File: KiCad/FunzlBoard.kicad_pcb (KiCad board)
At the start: 2 copper layers, 174 x 149 mm, 56 parts, among them U1 ESP32-C3_SUPERMINI_SMD, U2 ADS7828, U3 MCP23017_SO

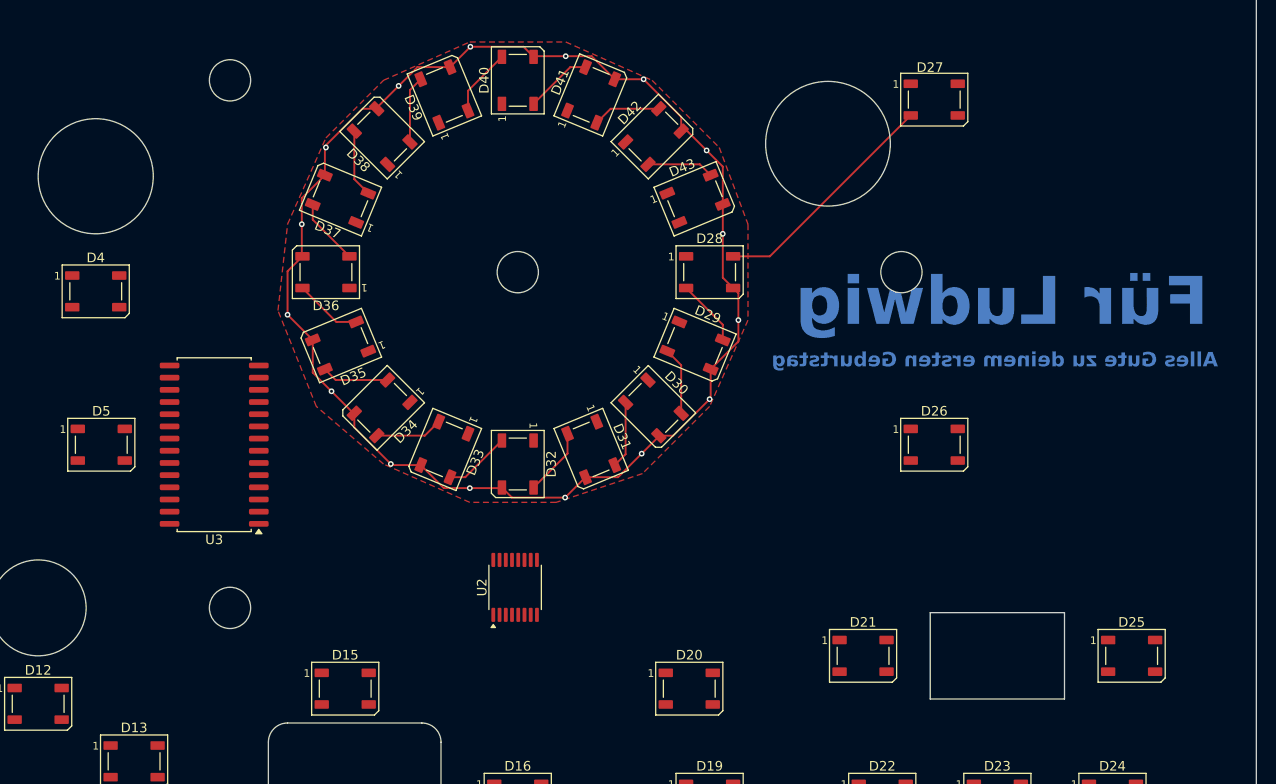
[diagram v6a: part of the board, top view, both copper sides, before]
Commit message: Add Color Buttons to PCB
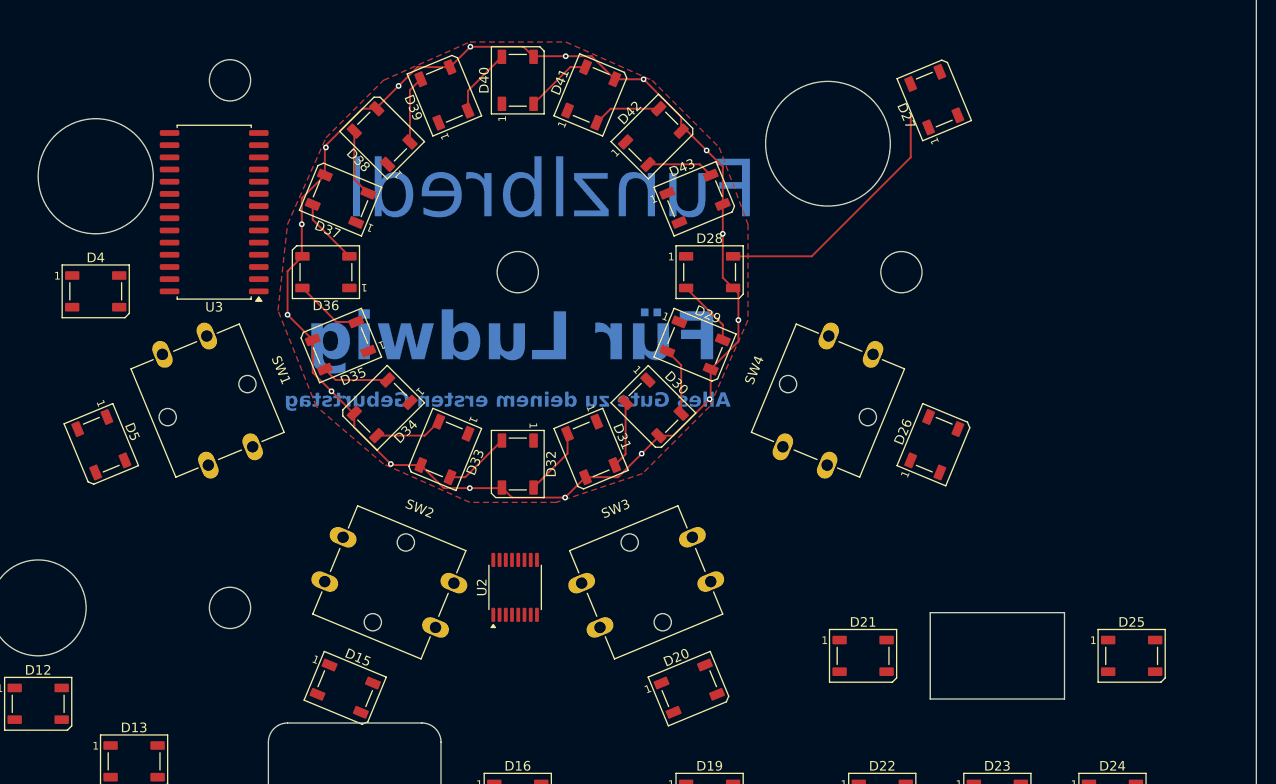
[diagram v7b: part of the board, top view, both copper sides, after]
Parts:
- added SW1: SW_MEC_5E, Lib:ColorButton, F.Cu at (67.7, 78.4)
- added SW2: SW_MEC_5E, Lib:ColorButton, F.Cu at (86.6, 97.3)
- added SW3: SW_MEC_5E, Lib:ColorButton, F.Cu at (113.4, 97.3)
- added SW4: SW_MEC_5E, Lib:ColorButton, F.Cu at (132.3, 78.4)
- moved U3 24.2 mm to (68.3, 58.7)
- turned D15 to -22.5 degrees
- turned D20 to 22.5 degrees
- turned D26 to 67.5 degrees
- turned D27 to 112.5 degrees
- turned D5 to -67.5 degrees
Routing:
- net Net-(D27-DOUT): track 24.6 -> 27.2 mm
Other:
- board text added: "Funzlbredl"

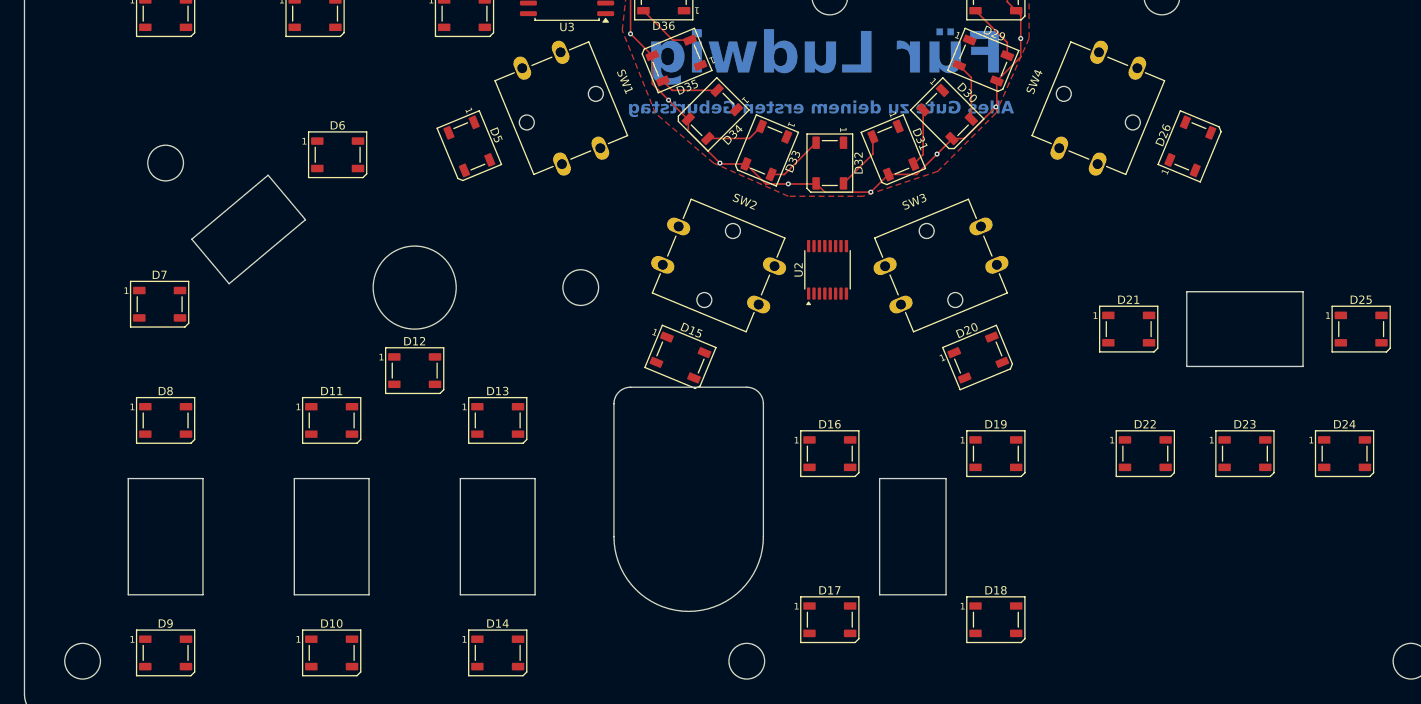
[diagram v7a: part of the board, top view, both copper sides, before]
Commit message: Add footprints for sliders
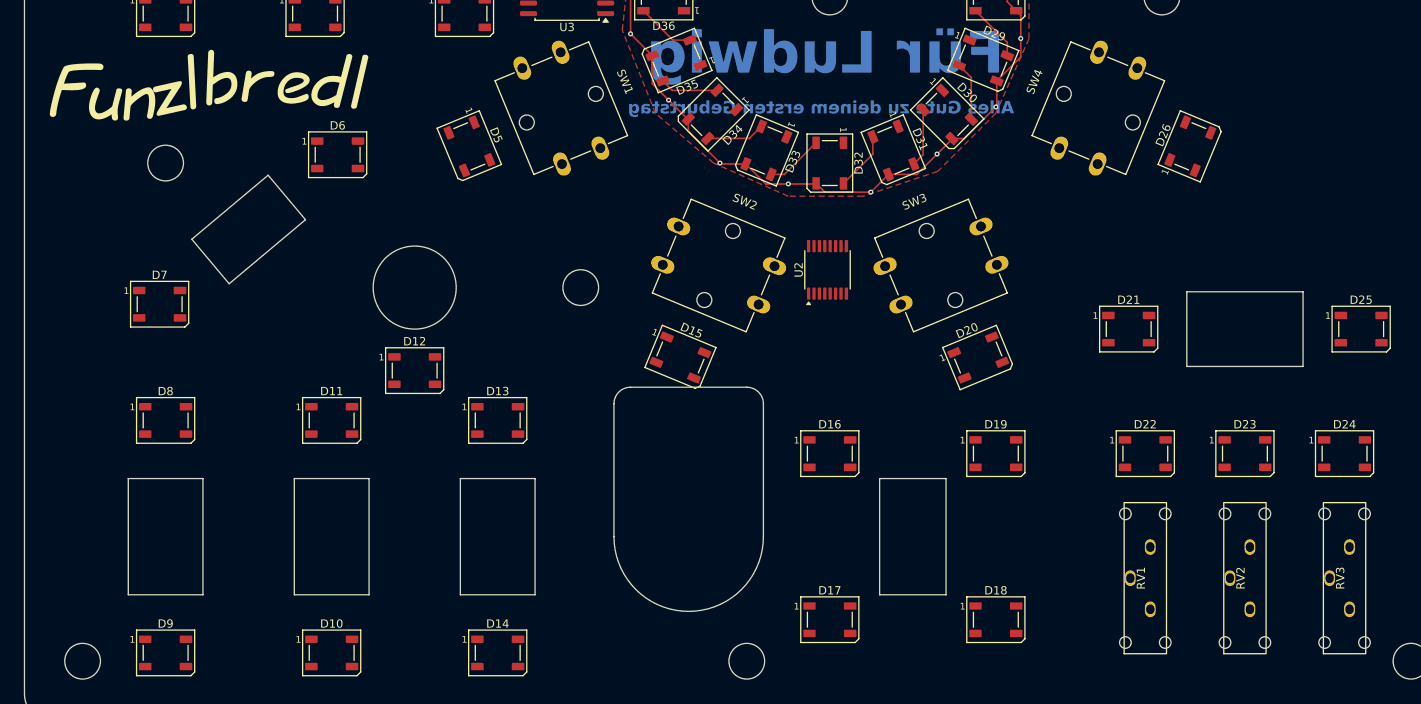
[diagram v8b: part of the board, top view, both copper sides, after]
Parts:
- added RV1: R_Potentiometer, Lib:Slider, F.Cu at (138.0, 135.0)
- added RV2: R_Potentiometer, Lib:Slider, F.Cu at (150.0, 135.0)
- added RV3: R_Potentiometer, Lib:Slider, F.Cu at (162.0, 135.0)
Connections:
- SW1 pad 2: unconnected-(SW1-Pad2) -> Net-(U3-GPB0)
- SW2 pad 2: unconnected-(SW2-Pad2) -> Net-(U3-GPB1)
- SW3 pad 2: unconnected-(SW3-Pad2) -> Net-(U3-GPB2)
- SW4 pad 2: unconnected-(SW4-Pad2) -> Net-(U3-GPB3)
- U2 pad 1: unconnected-(U2-CH0-Pad1) -> Net-(U2-CH0)
- U2 pad 2: unconnected-(U2-CH1-Pad2) -> Net-(U2-CH1)
- U2 pad 3: unconnected-(U2-CH2-Pad3) -> Net-(U2-CH2)
- U2 pad 4: unconnected-(U2-CH3-Pad4) -> Net-(U2-CH3)
- U2 pad 5: unconnected-(U2-CH4-Pad5) -> Net-(U2-CH4)
- U2 pad 7: unconnected-(U2-CH6-Pad7) -> +3V3
- U2 pad 8: unconnected-(U2-CH7-Pad8) -> GND
- U3 pad 1: unconnected-(U3-GPB0-Pad1) -> Net-(U3-GPB0)
- U3 pad 2: unconnected-(U3-GPB1-Pad2) -> Net-(U3-GPB1)
- U3 pad 3: unconnected-(U3-GPB2-Pad3) -> Net-(U3-GPB2)
- U3 pad 4: unconnected-(U3-GPB3-Pad4) -> Net-(U3-GPB3)
